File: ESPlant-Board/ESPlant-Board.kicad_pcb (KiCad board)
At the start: 2 copper layers, 22 x 127 mm, 29 parts, among them J1 Conn_01x05, U1 ESP32-S2-MINI-1-N4, U3 Reset, U4 Boot, U5 Temp/Humid-Sensor, U6 Light sensor, U7 AMS1117-3_3, U8 MK-12C02-G025

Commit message: Board: Update panel
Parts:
- added REF**: Tab_5mm, PCM_kikit:Tab_5mm, F.Cu at (254.9, 163.2)
- added REF**: Tab_5mm, PCM_kikit:Tab_5mm, F.Cu at (259.9, 136.1)
- added REF**: Tab_5mm, PCM_kikit:Tab_5mm, F.Cu at (237.1, 136.1)
- added REF**: Tab_5mm, PCM_kikit:Tab_5mm, F.Cu at (259.9, 118.3)
- added REF**: Tab_5mm, PCM_kikit:Tab_5mm, F.Cu at (259.9, 147.1)
- added REF**: Tab_5mm, PCM_kikit:Tab_5mm, F.Cu at (237.1, 147.1)
- added REF**: Tab_5mm, PCM_kikit:Tab_5mm, F.Cu at (242.1, 163.2)
- added REF**: Tab_5mm, PCM_kikit:Tab_5mm, F.Cu at (260.0, 102.7)
- added REF**: Tab_5mm, PCM_kikit:Tab_5mm, F.Cu at (237.1, 118.3)
- added REF**: Tab_5mm, PCM_kikit:Tab_5mm, F.Cu at (237.1, 102.7)
- moved C7 1.50 mm to (253.4, 119.0)
- moved C5 1.18 mm to (256.0, 117.7)
- moved R1 1.18 mm to (255.9, 116.7)
- moved R3 1.18 mm to (255.9, 118.7)
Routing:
- net /Light_Sensor_Select_1: track 7.01 -> 6.14 mm
- net /Light_Sensor_Select_2: track 7.37 -> 7.98 mm
- net /Light_Sensor_Analog: track 39.5 -> 39.0 mm

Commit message: board, case: more work
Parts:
- moved REF** 0.80 mm to (259.9, 103.5)
- moved REF** 0.80 mm to (237.1, 103.5)
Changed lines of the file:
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@@
   )
   (footprint "PCM_kikit:Tab_5mm" (layer "F.Cu")
-    (at 259.99 102.7 180)
+    (at 259.94 103.5 180)
     (descr "A symbol representing annotation for tab placement")
     (attr exclude_from_pos_files exclude_from_bom)
@@
   )
   (footprint "PCM_kikit:Tab_5mm" (layer "F.Cu")
-    (at 237.09 102.7)
+    (at 237.14 103.5)
     (descr "A symbol representing annotation for tab placement")
     (attr exclude_from_pos_files exclude_from_bom)

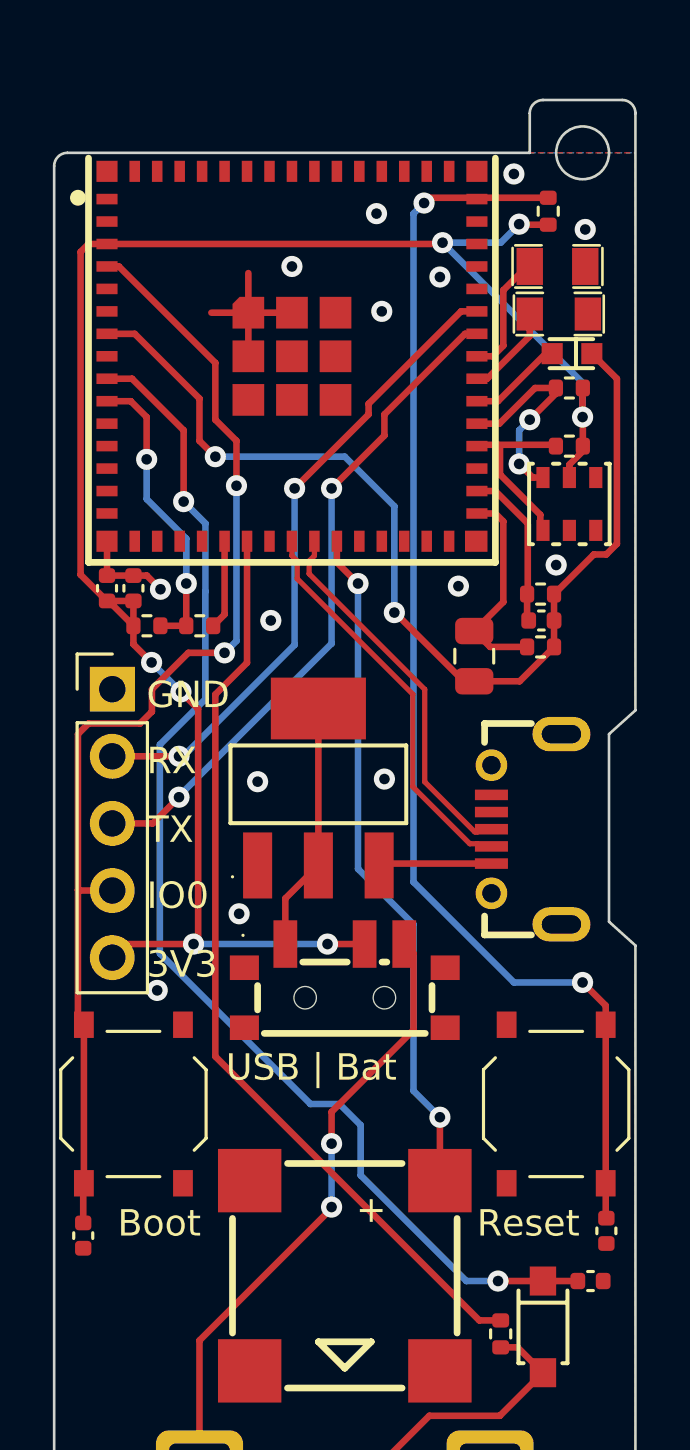
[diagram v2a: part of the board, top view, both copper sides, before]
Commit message: Board: changed to esp32-c6-mini-1-n4
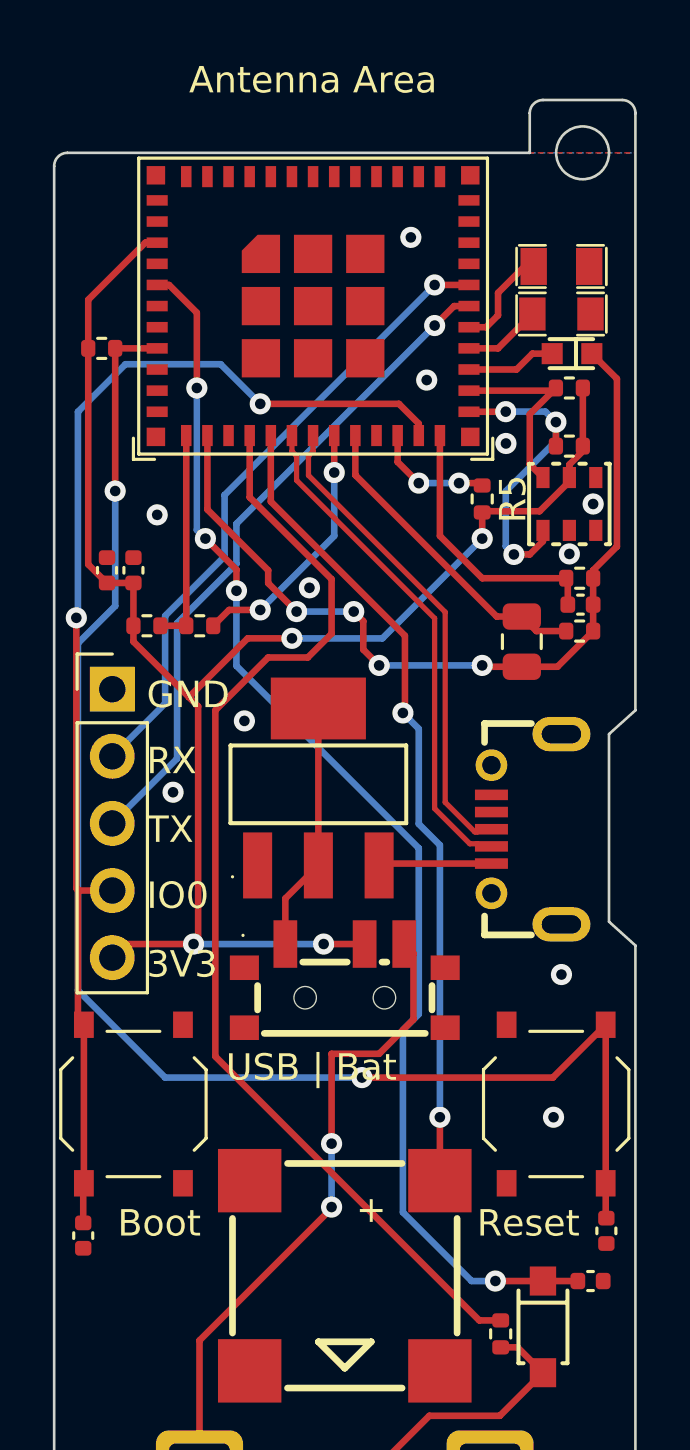
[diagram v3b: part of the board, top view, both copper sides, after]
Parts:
- removed REF** (x10): Tab_5mm, PCM_kikit:Tab_5mm
- added R5: 10k, Resistor_SMD:R_0402_1005Metric, F.Cu at (253.7, 113.1)
- U1: value ESP32-S2-MINI-1-N4 -> ESP32-C6-MINI-1/U; footprint CustomFootprints:WIFI-SMD_ESP32-MINI-1-N4 -> Espressif:ESP32-C6-MINI-1
- moved R9 17.7 mm to (239.3, 107.4), turned to 0 degrees
- moved U1 4.67 mm to (247.3, 103.1)
- moved C7 1.88 mm to (255.2, 118.5)
- moved R1 1.60 mm to (257.4, 116.1)
- moved R3 1.60 mm to (257.4, 118.1)
- moved C5 1.60 mm to (257.5, 117.1)
- moved C8 0.68 mm to (240.5, 115.8)
- moved C9 0.68 mm to (239.5, 115.8)
- moved D1 0.15 mm to (256.7, 104.3)
- moved D3 0.10 mm to (256.7, 106.1)
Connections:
- C2 pad 2: /IO0 -> /IO9
- J1 pad 2: /RX -> /TX
- J1 pad 3: /TX -> /RX
- J1 pad 4: /IO0 -> /IO9
- R9 pad 1: /EN -> +3V3
- R9 pad 2: +3V3 -> /EN
- U1 pad 10: /Voltage_Measurement_Analog -> unconnected-(U1-MTDI/GPIO5/ADC1_CH5-Pad10)
- U1 pad 11: unconnected-(U1-IO7-Pad11) -> GND
- U1 pad 12: unconnected-(U1-IO8-Pad12) -> /Voltage_Measurement_Analog
- U1 pad 13: unconnected-(U1-IO9-Pad13) -> /Light_Sensor_Analog
- U1 pad 14: unconnected-(U1-IO10-Pad14) -> GND
- U1 pad 15: unconnected-(U1-IO11-Pad15) -> /Square_Wave_Signal
- U1 pad 16: unconnected-(U1-IO12-Pad16) -> /Buzzer
- U1 pad 17: unconnected-(U1-IO13-Pad17) -> /D-
- U1 pad 18: unconnected-(U1-IO14-Pad18) -> /D+
- U1 pad 19: unconnected-(U1-IO15-Pad19) -> /Voltage_Measurement_Select
- U1 pad 20: /Voltage_Measurement_Select -> /Light_Sensor_Select_2
- U1 pad 21: /Square_Wave_Signal -> unconnected-(U1-NC-Pad21)
- U1 pad 22: unconnected-(U1-IO18-Pad22) -> /IO8
- U1 pad 23: /D- -> /IO9
- U1 pad 24: /D+ -> /Light_Sensor_Select_1
- U1 pad 25: /Buzzer -> /TH_SDA
- U1 pad 26: unconnected-(U1-IO26-Pad26) -> /TH_SCL
- U1 pad 27: unconnected-(U1-NC-Pad27) -> /Light_Sensor_In
- U1 pad 28: unconnected-(U1-IO33-Pad28) -> /LED_RED
- U1 pad 29: unconnected-(U1-IO34-Pad29) -> /LED_GREEN
- U1 pad 30: GND -> /RX
- U1 pad 31: /Light_Sensor_Select_2 -> /TX
- U1 pad 32: /Light_Sensor_Select_1 -> unconnected-(U1-NC-Pad32)
- U1 pad 34: /TH_SDA -> unconnected-(U1-NC-Pad34)
- U1 pad 35: /TH_SCL -> unconnected-(U1-NC-Pad35)
- U1 pad 36: /Light_Sensor_In -> GND
- U1 pad 37: /LED_RED -> GND
- U1 pad 38: /LED_GREEN -> GND
- U1 pad 39: /TX -> GND
- U1 pad 4: /IO0 -> unconnected-(U1-NC-Pad4)
- U1 pad 40: /RX -> GND
- U1 pad 41: unconnected-(U1-IO45-Pad41) -> GND
- U1 pad 44: unconnected-(U1-IO46-Pad44) -> GND
- U1 pad 45: /EN -> GND
- U1 pad 5: unconnected-(U1-IO1-Pad5) -> /AD_Capacitance
- U1 pad 7: /Light_Sensor_Analog -> unconnected-(U1-NC-Pad7)
- U1 pad 8: unconnected-(U1-IO4-Pad8) -> /EN
- U1 pad 9: /AD_Capacitance -> unconnected-(U1-MTMS/GPIO4/ADC1_CH4-Pad9)
- U4 pad 2: /IO0 -> /IO9
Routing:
- net /IO9: track 0.00 -> 47.2 mm, vias 0 -> 2
- net /IO0: track 44.3 -> 0.00 mm, vias 2 -> 0
- net GND: track 9.77 -> 0.04 mm, vias 17 -> 14
- net +3V3: track 70.4 -> 62.1 mm, vias 7 -> 4
- net /EN: track 47.9 -> 56.0 mm
- net /Square_Wave_Signal: track 34.9 -> 42.4 mm
- net /Voltage_Measurement_Select: track 3.38 -> 9.79 mm, vias 0 -> 2
- net /Light_Sensor_Analog: track 39.0 -> 32.6 mm, vias 2 -> 4
- net /TH_SDA: track 6.93 -> 12.0 mm, vias 0 -> 3
- net /Buzzer: track 25.9 -> 30.9 mm
- net /IO8: track 0.00 -> 4.57 mm, vias 0 -> 2
- net /Light_Sensor_Select_1: track 6.14 -> 10.3 mm
- net /D+: track 14.4 -> 18.4 mm
- net /D-: track 15.1 -> 19.1 mm
- net /Light_Sensor_Select_2: track 7.98 -> 11.9 mm
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
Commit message: Board: Add panel for esp32-c6
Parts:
- added REF**: Tab_5mm, PCM_kikit:Tab_5mm, F.Cu at (237.2, 146.8)
- added REF**: Tab_5mm, PCM_kikit:Tab_5mm, F.Cu at (260.0, 146.8)
- added REF**: Tab_5mm, PCM_kikit:Tab_5mm, F.Cu at (237.2, 103.5)
- added REF**: Tab_5mm, PCM_kikit:Tab_5mm, F.Cu at (260.0, 118.3)
- added REF**: Tab_5mm, PCM_kikit:Tab_5mm, F.Cu at (259.9, 103.5)
- added REF**: Tab_5mm, PCM_kikit:Tab_5mm, F.Cu at (237.1, 118.3)

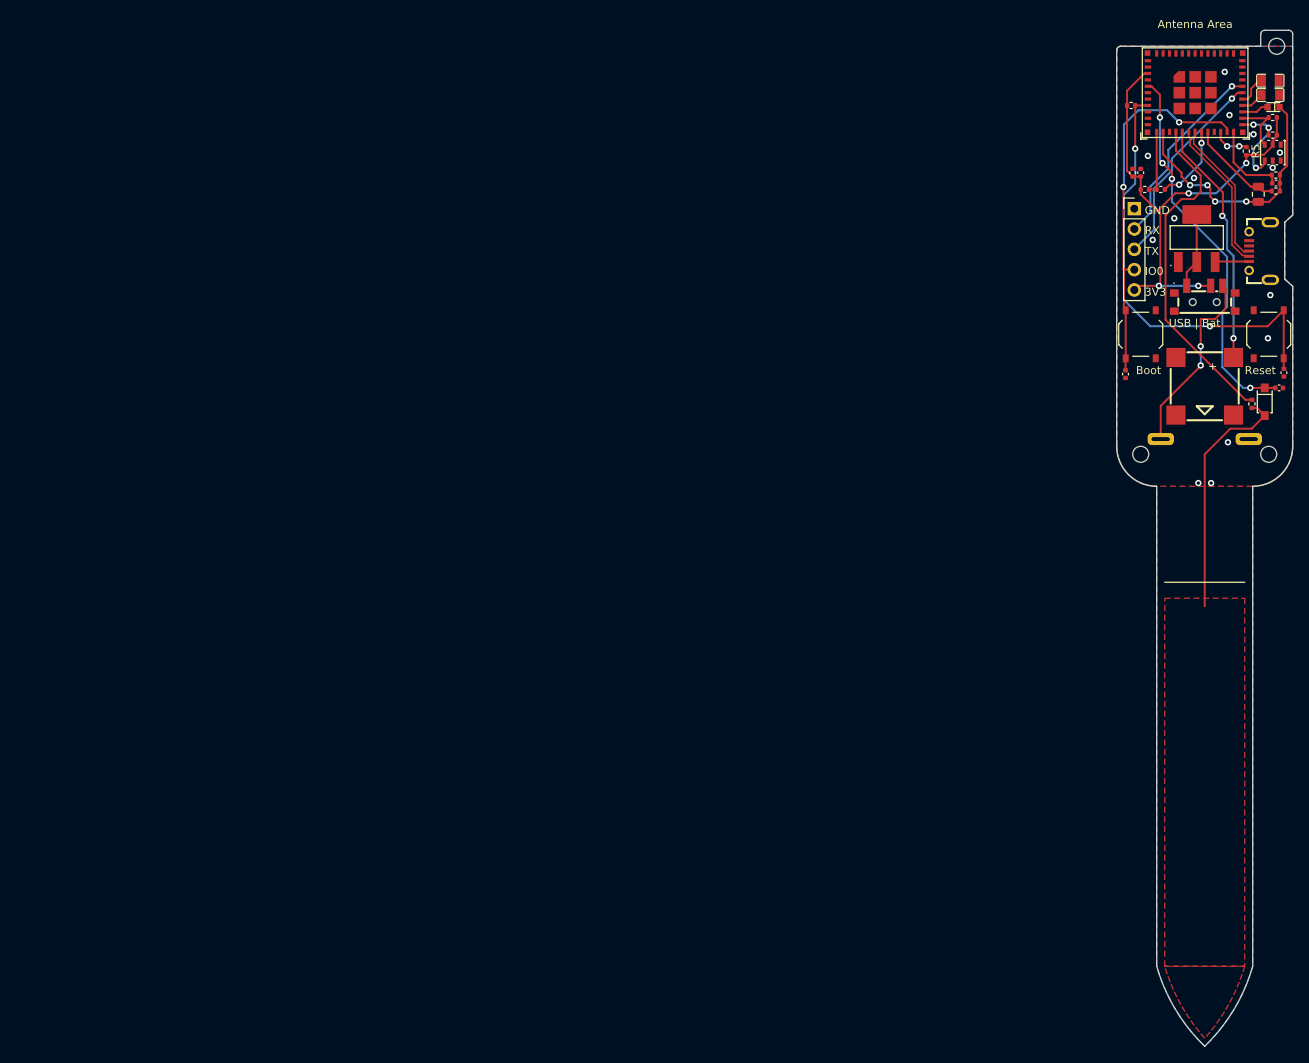
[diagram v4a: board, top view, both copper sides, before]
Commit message: Case: Add v2 case with improved folder structure
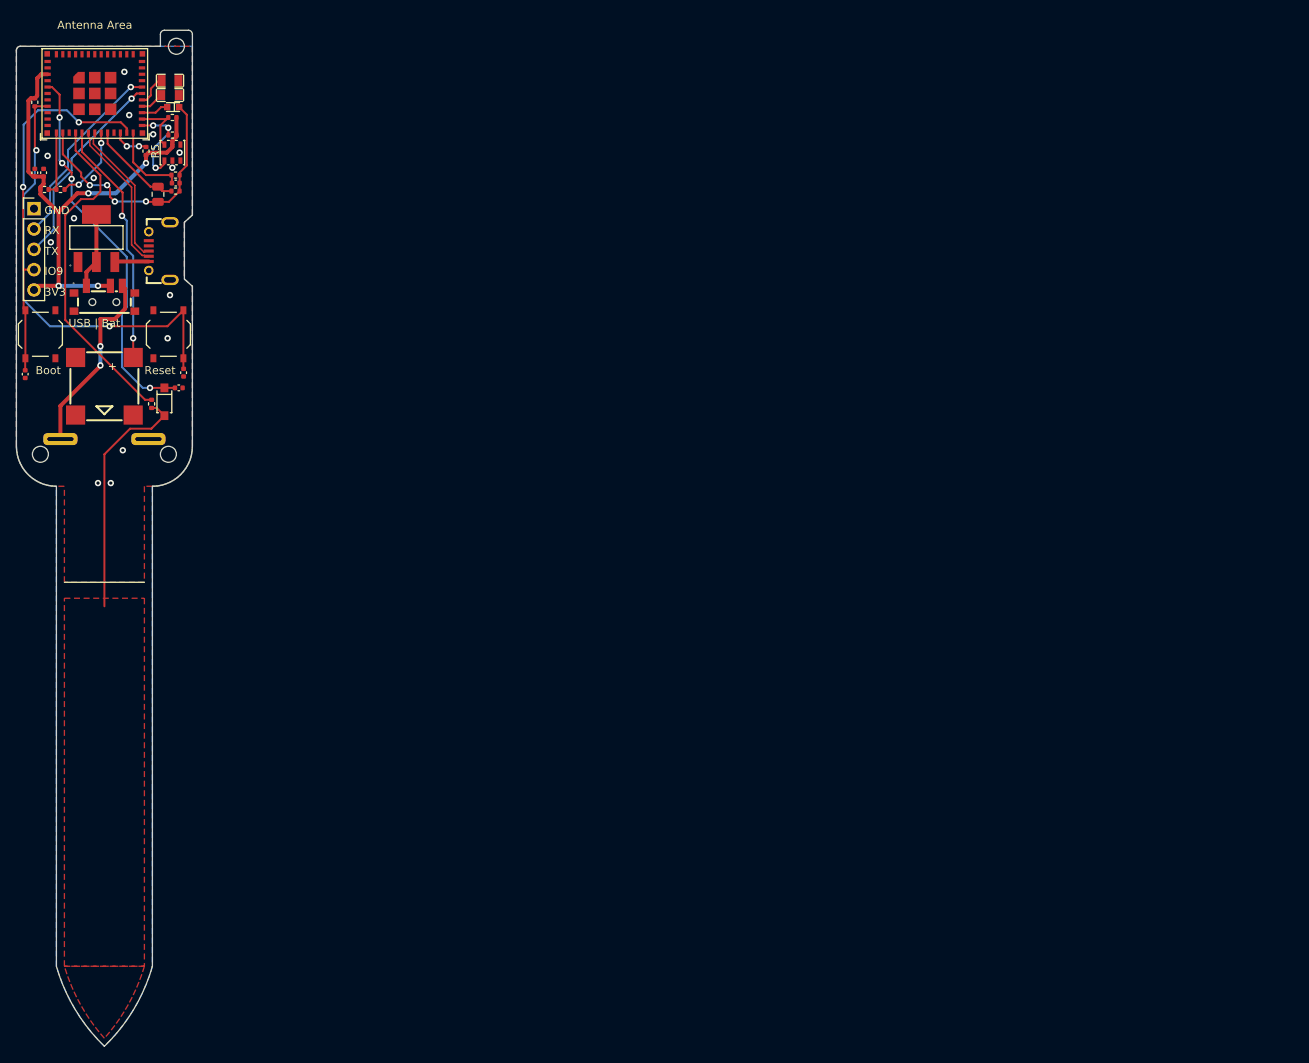
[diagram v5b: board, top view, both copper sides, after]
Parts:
- moved U1 137.5 mm to (109.8, 103.2)
- moved C7 137.5 mm to (117.7, 118.5)
- moved D1 137.5 mm to (119.2, 104.3)
- moved D2 137.5 mm to (118.5, 144.4)
- moved D3 137.5 mm to (119.2, 106.1)
- moved J1 137.5 mm to (102.2, 120.3)
- moved R1 137.5 mm to (119.9, 116.1)
- moved R10 137.5 mm to (119.5, 111.1)
- moved R2 137.5 mm to (119.5, 108.9)
- moved R3 137.5 mm to (119.9, 118.1)
- moved R4 137.5 mm to (103.5, 117.9)
- moved R5 137.5 mm to (116.2, 113.1)
- moved R6 137.5 mm to (105.5, 117.9)
- moved REF** 137.5 mm to (122.5, 146.8)
- moved REF** 137.5 mm to (99.7, 103.5)
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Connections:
- net Net-(U7-VOUT-Pad2) renamed /USB
- net Net-(U9-+) renamed /BAT
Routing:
- net +3V3: track 62.1 -> 62.7 mm
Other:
- board text added: "IO9"
- board text removed: "IO0"

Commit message: Finish v2.0 for prototyping
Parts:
- moved REF** 0.40 mm to (99.7, 103.9)
- moved REF** 0.40 mm to (122.4, 103.9)
- moved REF** 0.30 mm to (99.7, 146.5)
- moved REF** 0.30 mm to (122.5, 146.5)
- moved REF** 0.30 mm to (122.5, 118.0)
- moved REF** 0.30 mm to (99.5, 118.0)
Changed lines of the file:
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@@
   )
   (footprint "PCM_kikit:Tab_5mm" (layer "F.Cu")
-    (at 99.65 146.8)
+    (at 99.65 146.5)
     (descr "A symbol representing annotation for tab placement")
     (attr exclude_from_pos_files exclude_from_bom)
@@
   )
   (footprint "PCM_kikit:Tab_5mm" (layer "F.Cu")
-    (at 122.45 146.8 180)
+    (at 122.45 146.5 180)
     (descr "A symbol representing annotation for tab placement")
     (attr exclude_from_pos_files exclude_from_bom)
@@
   )
   (footprint "PCM_kikit:Tab_5mm" (layer "F.Cu")
-    (at 99.7 103.5)
+    (at 99.7 103.9)
     (descr "A symbol representing annotation for tab placement")
     (attr exclude_from_pos_files exclude_from_bom)
@@
   )
   (footprint "PCM_kikit:Tab_5mm" (layer "F.Cu")
-    (at 122.45 118.3 180)
+    (at 122.45 118 180)
     (descr "A symbol representing annotation for tab placement")
     (attr exclude_from_pos_files exclude_from_bom)
@@
   )
   (footprint "PCM_kikit:Tab_5mm" (layer "F.Cu")
-    (at 122.4 103.5 180)
+    (at 122.4 103.9 180)
     (descr "A symbol representing annotation for tab placement")
     (attr exclude_from_pos_files exclude_from_bom)
@@
   )
   (footprint "PCM_kikit:Tab_5mm" (layer "F.Cu")
-    (at 99.55 118.3)
+    (at 99.55 118)
     (descr "A symbol representing annotation for tab placement")
     (attr exclude_from_pos_files exclude_from_bom)
@@
   (via (at 111.650006 135) (size 0.8) (drill 0.4) (layers "F.Cu" "B.Cu") (net 1))
   (via (at 102.5 113) (size 0.8) (drill 0.4) (layers "F.Cu" "B.Cu") (net 1))
-  (segment (start 102.31 113.19) (end 102.31 117.152653) (width 0.25) (layer "B.Cu") (net 1))
-  (segment (start 100.9 118.562653) (end 100.9 131.7) (width 0.25) (layer "B.Cu") (net 1))
-  (segment (start 102.31 117.152653) (end 100.9 118.562653) (width 0.25) (layer "B.Cu") (net 1))
   (segment (start 104.2 135) (end 111.650006 135) (width 0.25) (layer "B.Cu") (net 1))
+  (segment (start 102.31 117.771326) (end 100.9 119.181326) (width 0.25) (layer "B.Cu") (net 1))
+  (segment (start 102.5 113) (end 102.31 113.19) (width 0.25) (layer "B.Cu") (net 1))
   (segment (start 100.9 131.7) (end 104.2 135) (width 0.25) (layer "B.Cu") (net 1))
-  (segment (start 102.5 113) (end 102.31 113.19) (width 0.25) (layer "B.Cu") (net 1))
+  (segment (start 100.9 119.181326) (end 100.9 131.7) (width 0.25) (layer "B.Cu") (net 1))
+  (segment (start 102.31 113.19) (end 102.31 117.771326) (width 0.25) (layer "B.Cu") (net 1))
   (segment (start 106.9 115.7755) (end 105.7245 114.6) (width 0.25) (layer "F.Cu") (net 2))
   (segment (start 105.4 108.9) (end 105.4 106.05) (width 0.25) (layer "F.Cu") (net 2))
@@
   (via (at 110.5 137.5) (size 0.8) (drill 0.4) (layers "F.Cu" "B.Cu") (net 31))
   (segment (start 110.5 139.9) (end 110.5 137.5) (width 0.5) (layer "B.Cu") (net 31))
-  (segment (start 100.84 117.6) (end 100.84 127.84) (width 0.25) (layer "F.Cu") (net 32))
   (segment (start 101.1 140.5) (end 101.1 139.025) (width 0.25) (layer "F.Cu") (net 32))
   (segment (start 100.9 127.9) (end 100.92 127.92) (width 0.25) (layer "F.Cu") (net 32))
@@
   (segment (start 101.125 133) (end 100.9 132.775) (width 0.25) (layer "F.Cu") (net 32))
   (segment (start 113.8 110.25) (end 113.8 110.8) (width 0.25) (layer "F.Cu") (net 32))
-  (segment (start 100.839027 117.599027) (end 100.84 117.6) (width 0.25) (layer "F.Cu") (net 32))
+  (segment (start 100.84 118.216728) (end 100.84 127.84) (width 0.25) (layer "F.Cu") (net 32))
+  (segment (start 101.428364 117.628364) (end 100.84 118.216728) (width 0.25) (layer "F.Cu") (net 32))
+  (segment (start 100.84 127.84) (end 100.9 127.9) (width 0.25) (layer "F.Cu") (net 32))
   (segment (start 100.9 132.775) (end 100.9 127.9) (width 0.25) (layer "F.Cu") (net 32))
-  (segment (start 100.84 127.84) (end 100.9 127.9) (width 0.25) (layer "F.Cu") (net 32))
-  (via (at 100.839027 117.599027) (size 0.8) (drill 0.4) (layers "F.Cu" "B.Cu") (net 32))
+  (via (at 101.428364 117.628364) (size 0.8) (drill 0.4) (layers "F.Cu" "B.Cu") (net 32))
   (via (at 107.8 109.5) (size 0.8) (drill 0.4) (layers "F.Cu" "B.Cu") (net 32))
+  (segment (start 101.428364 117.628364) (end 100.9 117.1) (width 0.25) (layer "B.Cu") (net 32))
   (segment (start 106.3 108) (end 107.8 109.5) (width 0.25) (layer "B.Cu") (net 32))
-  (segment (start 100.9 117.538054) (end 100.9 109.8) (width 0.25) (layer "B.Cu") (net 32))
   (segment (start 100.9 109.8) (end 102.7 108) (width 0.25) (layer "B.Cu") (net 32))
+  (segment (start 100.9 117.1) (end 100.9 109.8) (width 0.25) (layer "B.Cu") (net 32))
   (segment (start 102.7 108) (end 106.3 108) (width 0.25) (layer "B.Cu") (net 32))
-  (segment (start 100.839027 117.599027) (end 100.9 117.538054) (width 0.25) (layer "B.Cu") (net 32))
   (segment (start 113 111.7) (end 113 110.8) (width 0.25) (layer "F.Cu") (net 43))
   (segment (start 116.11 112.5) (end 116.2 112.59) (width 0.25) (layer "F.Cu") (net 43))
